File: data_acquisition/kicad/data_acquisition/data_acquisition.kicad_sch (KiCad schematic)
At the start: 9 parts, among them J1 7-12V Sensor Socket, J2 Conn_01x02_Pin, J3 Ultrasonic Sensor Socket, J4 Conn_01x04_Pin, J5 RS485 Breakout Socket, J6 Conn_01x03_Pin, U1 ESP32-C5-DevKitC-1

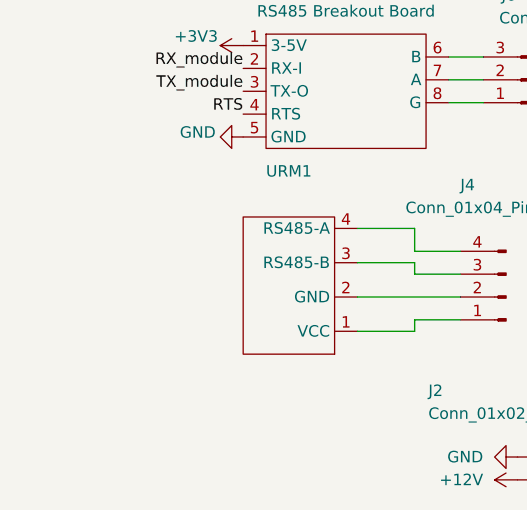
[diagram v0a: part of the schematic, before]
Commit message: Adding wire color legend
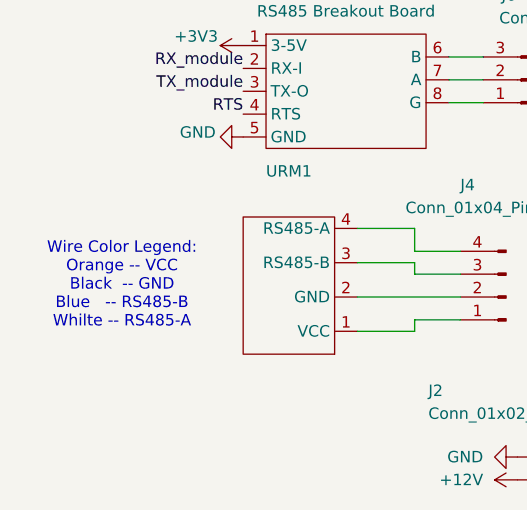
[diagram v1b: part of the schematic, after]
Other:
- note added: "Wire Color Legend: Orange -- VCC Black -- GND Blue -- RS485-B Whilte -- RS485-A"
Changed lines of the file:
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@@
 		(comment 3 "It will send data to another ESP32 using ESP-NOW")
+	)
+	(text "Wire Color Legend:\nOrange -- VCC\nBlack  -- GND\nBlue   -- RS485-B\nWhilte -- RS485-A\n"
+		(exclude_from_sim no)
+		(at 27.178 101.6 0)
+		(effects
+			(font
+				(size 1.27 1.27)
+			)
+		)
 	)
 	(text "Note:\nTX (module) <--> RX (ESP32)\nRX (module) <--> TX (ESP32)"
